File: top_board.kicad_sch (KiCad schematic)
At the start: 16 parts, among them U10 74LS00, U11 74LS32, U12 74LS86, U13 74LS166, U14 74LS374, U15 74LS138, U16 74LS257, U17 74LS257, U18 74LS257, U19 74LS257

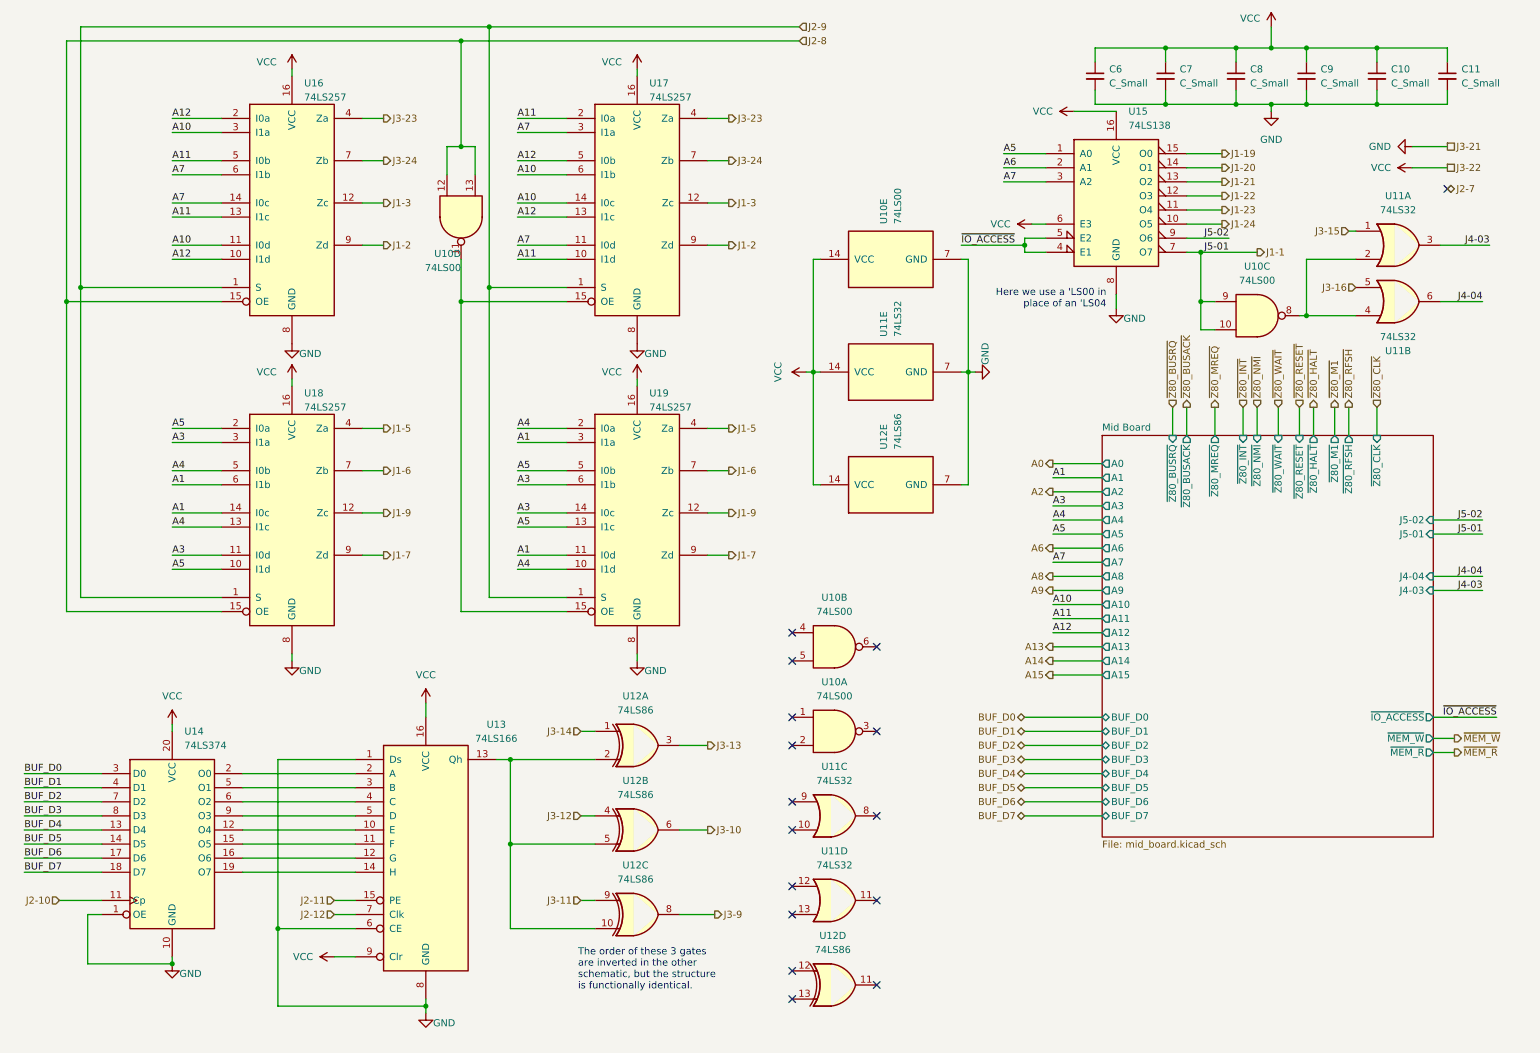
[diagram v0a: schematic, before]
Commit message: Added some basic traces for power
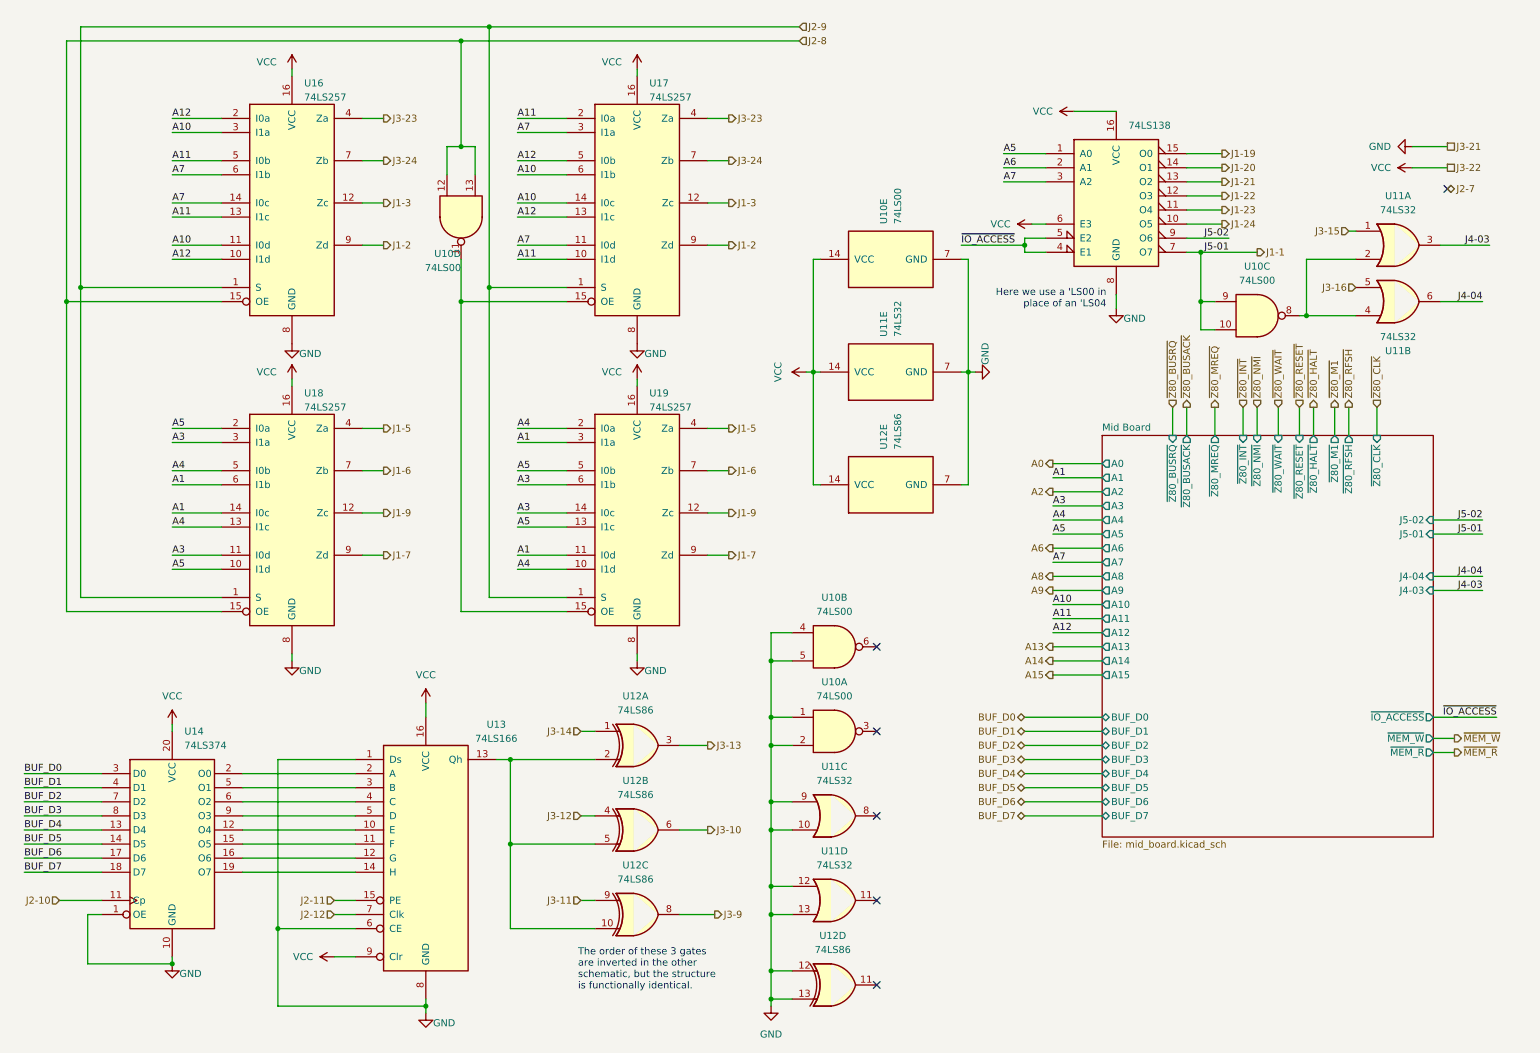
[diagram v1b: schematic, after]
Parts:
- removed C10, C11, C6, C7, C8, C9: C_Small, symbol Device:C_Small
- U10, U11, U12: footprint (none) -> Package_SO:SOIC-14_3.9x8.7mm_P1.27mm
- U13, U15, U16, U17, U18, U19: footprint (none) -> Package_SO:SOIC-16_3.9x9.9mm_P1.27mm
- U14: footprint (none) -> Package_SO:SO-20_5.3x12.6mm_P1.27mm
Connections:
- net GND: now also U10.1, U10.2, U10.4, U10.5, U11.10, U11.12, U11.13, U11.9, U12.12, U12.13
- no-connect marks 16 -> 6

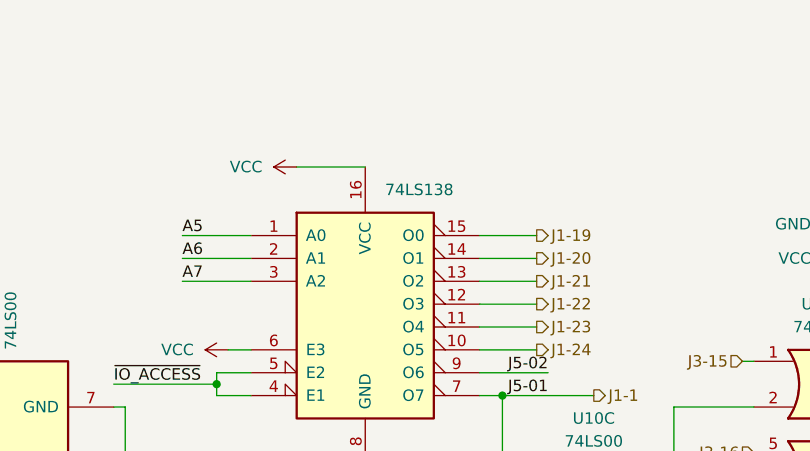
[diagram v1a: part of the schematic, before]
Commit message: Fix adder bit ordering
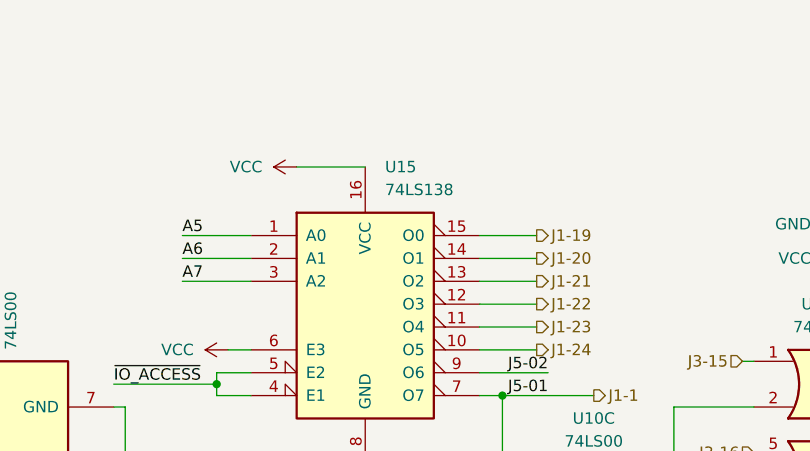
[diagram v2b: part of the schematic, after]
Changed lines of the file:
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@@
 				)
 				(justify left)
-				(hide yes)
 			)
 		)

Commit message: Removed some text from schematic, added some more, generate PDF
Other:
- note removed: "Here we use a 'LS00 in place of an 'LS04"
- note removed: "The order of these 3 gates are inverted in the other schematic, but the structure is functionally identical."
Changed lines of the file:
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@@
-		)
-	)
-	(text "The order of these 3 gates\nare inverted in the other\nschematic, but the structure\nis functionally identical."
-		(exclude_from_sim no)
-		(at 117.602 185.166 0)
-		(effects
-			(font
-				(size 1.27 1.27)
-			)
-			(justify left)
-		)
-	)
-	(text "Here we use a 'LS00 in\nplace of an 'LS04"
-		(exclude_from_sim no)
-		(at 212.852 64.262 0)
-		(effects
-			(font
-				(size 1.27 1.27)
-			)
-			(justify right)
 		)
 	)
